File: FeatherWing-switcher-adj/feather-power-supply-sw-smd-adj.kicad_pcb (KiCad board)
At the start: 2 copper layers, 19 parts, among them J2 Conn_01x16, J3 QWIIC, J4 0.1, Q1 Q_PMOS_GSD, U1 MCP16312MS

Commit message: minor board changes
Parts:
- moved C6 0.20 mm to (142.3, 91.6)

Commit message: minor updates to bom and layout
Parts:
- added R6: 1M, Resistor_SMD:R_0603_1608Metric_Pad1.05x0.95mm_HandSolder, F.Cu at (133.3, 72.0)
- C5, C6: footprint Capacitor_SMD:C_1206_3216Metric_Pad1.42x1.75mm_HandSolder -> Capacitor_SMD:C_0805_2012Metric_Pad1.15x1.40mm_HandSolder
- R2: value 150 -> 330
- R7: value 10K -> 100K
- moved R7 0.97 mm to (133.3, 70.4)
- moved C6 0.70 mm to (142.0, 91.0)
- moved C5 0.43 mm to (142.0, 89.1)

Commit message: update fb res val and inductor val
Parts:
- L1: value 22uH -> 27uH

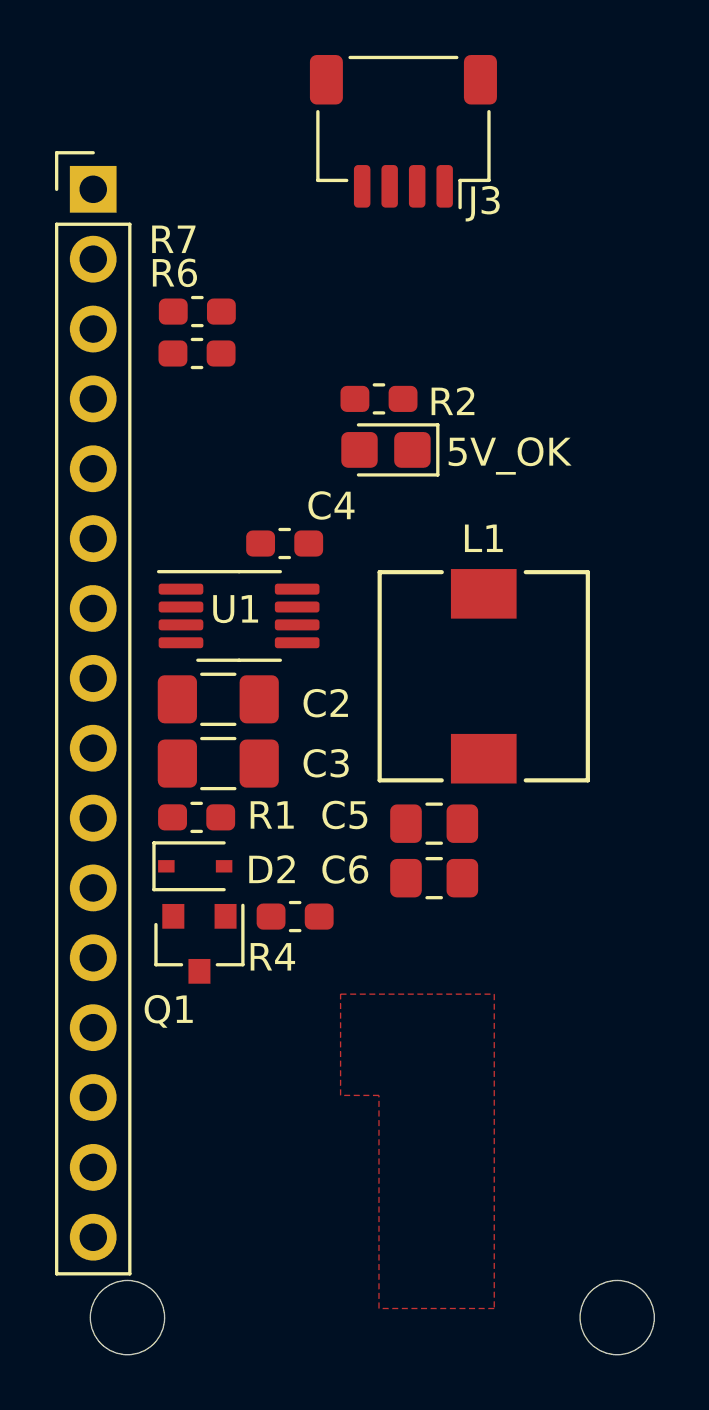
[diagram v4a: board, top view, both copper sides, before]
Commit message: update inductor and boms
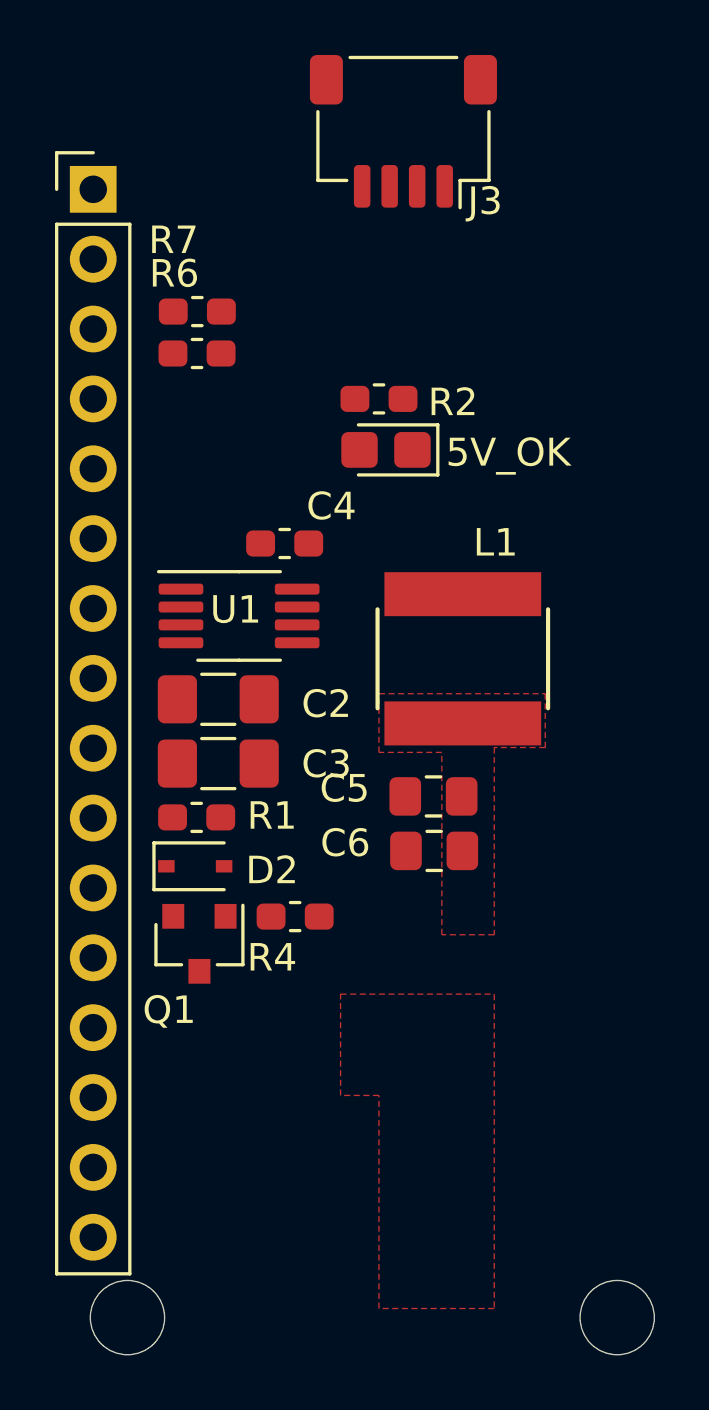
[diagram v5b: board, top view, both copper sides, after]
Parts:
- L1: footprint FeatherWing-switcher-adj:SRR7045-220M -> FeatherWing-switcher-adj:ASPI-6045S-270
- moved L1 0.99 mm to (143.0, 83.1)
- moved C5 0.99 mm to (141.9, 88.1)
- moved C6 0.99 mm to (142.0, 90.0)
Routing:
- added copper zone on F.Cu, net +5.3V
